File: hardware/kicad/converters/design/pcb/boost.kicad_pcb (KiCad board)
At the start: 2 copper layers, 120 x 56 mm, 11 parts, among them J1 lager ind (5V), J2 V2 ud (10V), J3 PWM (isoleret), J4 gate-forsyning, M1 IRF530, U1 4N25

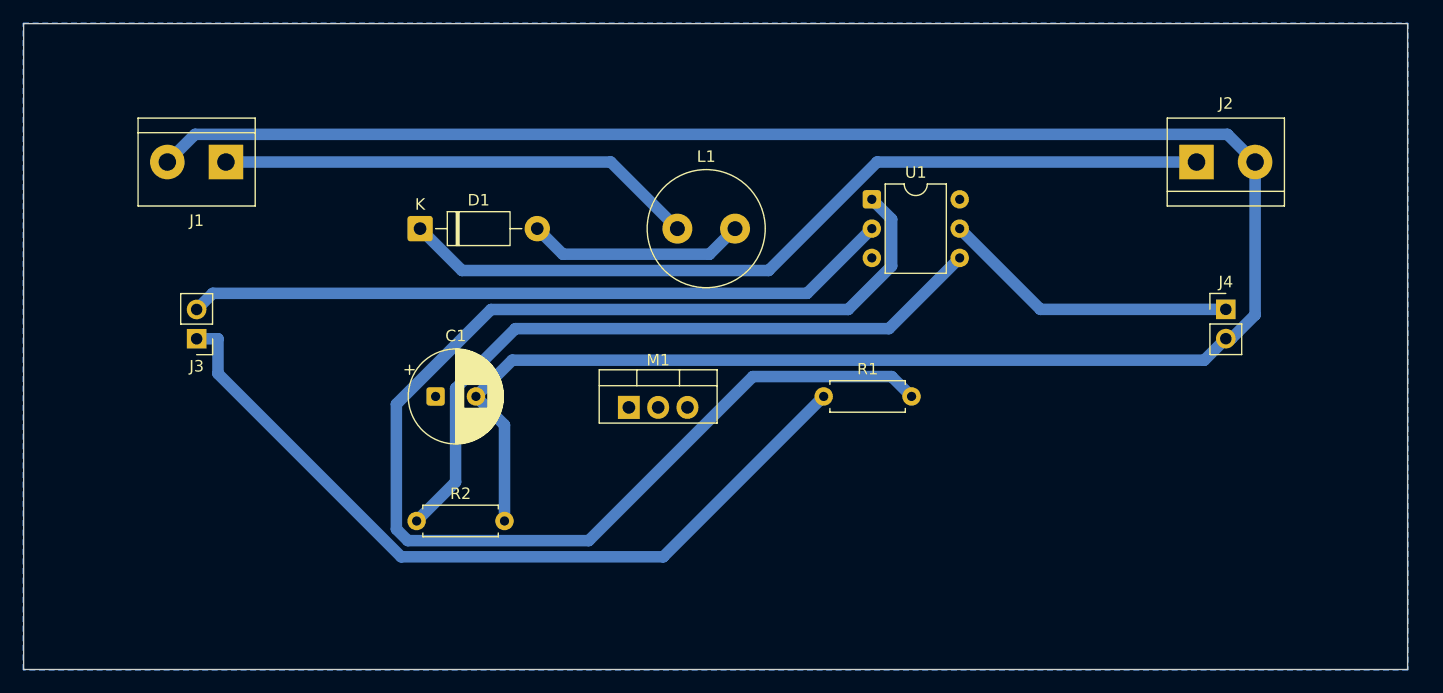
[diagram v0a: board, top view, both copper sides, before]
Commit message: Apply fiber-laser design rules from the DTU-PCB-prototyping guide
All seven boards rebuilt to meet the XTool fiber laser workflow
(SimsesLab/DTU-PCB-prototyping): 1.0 mm tracks, 0.8 mm clearance, solid
no-net fill zone on B.Cu (pad connection: none) so the laser only
engraves the isolation channels, DIP footprints switched to the
_LongPads variants from the guide's shop table.

TO packages cannot meet 0.8 mm pad-to-pad at stock sizes, so
energy_system.pretty now has TO-220-3_Vertical_LaserPads (pads narrowed
to 1.7 mm -> 0.84 mm gap; make_laserpads.py regenerates). The MPPT pass
transistor moves BD139 -> TIP41A (shop part): TO-126's 2.28 mm pitch can
never satisfy the rule, and TO-220 handles the ~7 W better anyway.

Two more bugs caught in this pass:
- Device:Q_NMOS uses letter pin numbers (G/D/S) while TO-220 pads are
  1/2/3 - buck/boost MOSFET pads silently got NO net in the earlier
  boards (no-net pads don't count as unconnected). pcb_build.py now maps
  G/D/S->1/2/3 and fails hard if a component ends up netless.
- DRC now 0 violations on all seven boards; remaining airwires are the
  documented jumpers.
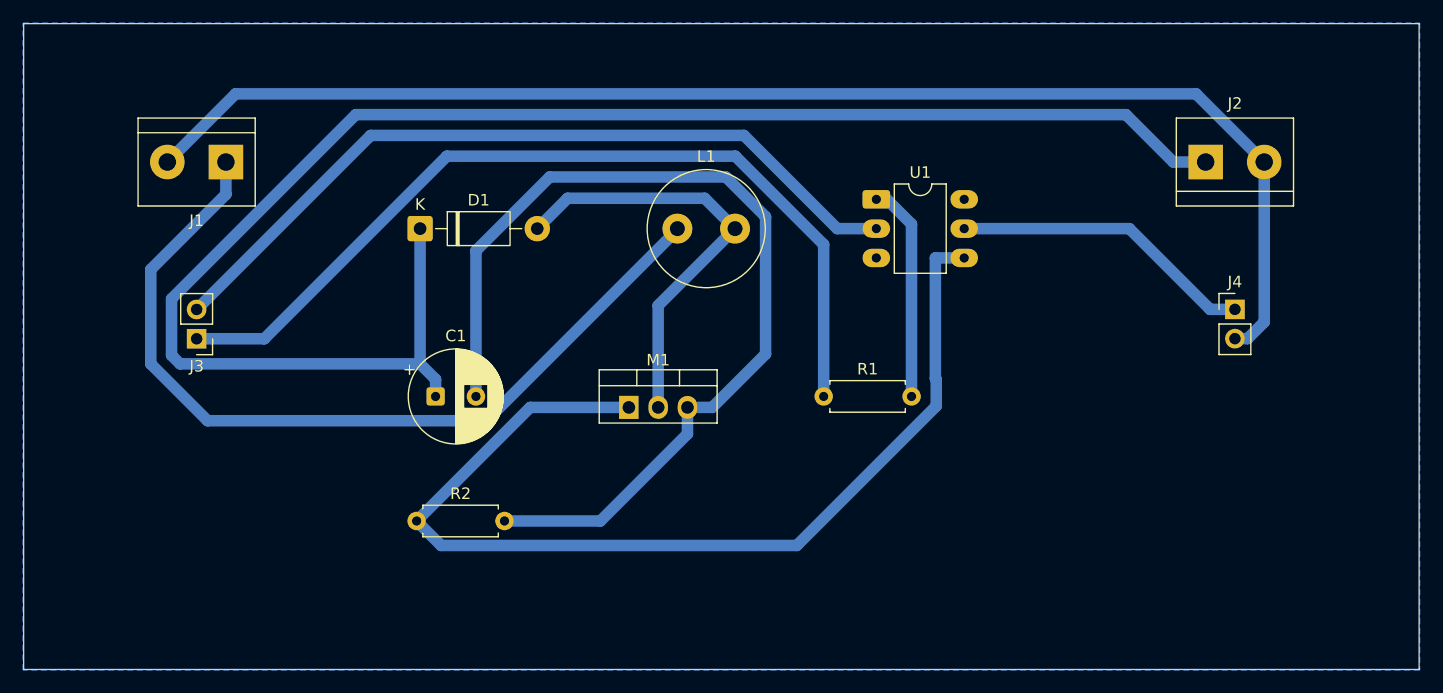
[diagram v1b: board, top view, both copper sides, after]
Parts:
- M1: footprint TO-220-3_Vertical -> TO-220-3_Vertical_LaserPads
- U1: footprint DIP-6_W7.62mm -> DIP-6_W7.62mm_LongPads
- moved J4 0.79 mm to (125.0, 44.8)
- moved J2 0.79 mm to (122.5, 32.0)
- moved U1 0.39 mm to (93.9, 35.2)
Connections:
- M1 pad 1: (no net) -> GATE
- M1 pad 2: (no net) -> Net-(D1-A)
- M1 pad 3: (no net) -> GND
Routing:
- net Net-(R1-Pad2): track 116.9 -> 18.9 mm
- net /VOUT_V2: track 72.7 -> 139.8 mm
- net /VIN_5V: track 41.5 -> 74.9 mm
- net GATE: track 61.3 -> 88.8 mm
- net Net-(D1-A): track 19.0 -> 37.6 mm
- net GND: track 191.9 -> 200.7 mm
- net PWM: track 69.7 -> 77.3 mm
- net GND_MCU: track 61.4 -> 68.5 mm
- added copper zone on B.Cu, net (none)
- removed copper zone on B.Cu, net GND
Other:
- board size 120 x 56 mm -> 121 x 56 mm

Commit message: Engrave component references into the copper on all boards
The fiber laser has no silkscreen step, so the refdes (R1, U1, ...) are
placed as mirrored copper text on B.Cu next to each component - they
engrave in the same run as the traces and read correctly from the
solder side. Placement is collision-checked against tracks/pads/other
text (copper text over a track would short or sever it); tracks are
sampled into small boxes so diagonal runs don't false-positive. 86 of
96 labels fit; the handful dropped in dense spots are listed in
production/README.md and still appear on the F_Fab plots.

Also exports <board>_silk_top.dxf (F.Silkscreen + outline) per board as
an optional top-side engraving pass - run it on the component side
BEFORE the copper run, and do NOT mirror that one.

DRC still 0 violations on all seven; jumper lists updated.
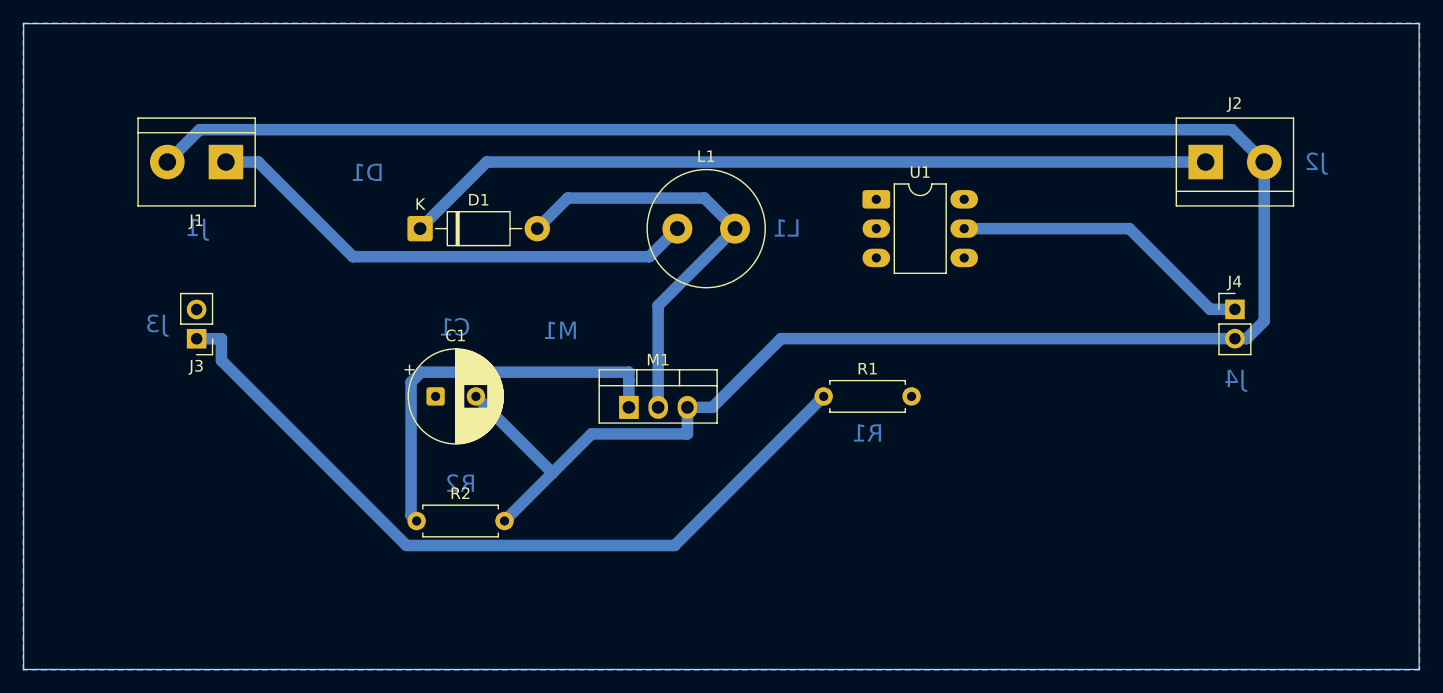
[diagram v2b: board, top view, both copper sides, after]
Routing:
- net /VOUT_V2: track 139.8 -> 70.5 mm
- net GND_MCU: track 68.5 -> 0.00 mm
- net GATE: track 88.8 -> 34.5 mm
- net /VIN_5V: track 74.9 -> 43.6 mm
- net Net-(R1-Pad2): track 18.9 -> 0.00 mm
- net PWM: track 77.3 -> 68.2 mm
- net GND: track 200.7 -> 195.0 mm
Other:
- board text added: "C1"
- board text added: "D1"
- board text added: "J1"
- board text added: "J2"
- board text added: "J3"
- board text added: "J4"
- board text added: "L1"
- board text added: "M1"
- board text added: "R1"
- board text added: "R2"
